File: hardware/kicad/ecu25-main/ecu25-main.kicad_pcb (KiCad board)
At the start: 2 copper layers, 200 x 150 mm, 303 parts, among them J1 Screw_Terminal_BATT, J10 Screw_Terminal_RS485, J11 TC2030 SWD, J12 Ribbon 20-way, J13 Screw_Terminal_DPLUS, J14 DEBUG_UART, J2 Screw_Terminal_DIN, J3 Screw_Terminal_SENDERS, J4 Screw_Terminal_MPU, J5 Screw_Terminal_GEN, J6 Screw_Terminal_MAINS, J7 Screw_Terminal_CT, J8 Screw_Terminal_RELAY_OUT, J9 Screw_Terminal_CAN, K1 G5LE-1 24V, K2 G5LE-1 24V, K3 G5LE-1 24V, K4 G5LE-1 24V, K5 G5LE-1 24V, K6 G5LE-1 24V, Q1 SQD50P06-15L, Q3 BC857, Q4 BC857, Q5 BC857, Q60 2N7002K 60V, Q61 2N7002K 60V, Q62 2N7002K 60V, Q63 2N7002K 60V, Q64 2N7002K 60V, Q65 2N7002K 60V, U1 LM5164DDA-Q1, U10 MCP6002, U11 M95M02-DR, U12 STM32F407VGT6, U2 TLV75533 (500mA), U3 LM358, U4 LM358, U5 LM2903, U6 TJA1051T/3, U7 THVD1450, U8 MCP6002, U9 MCP6002, Y1 8MHz, Y2 32.768kHz

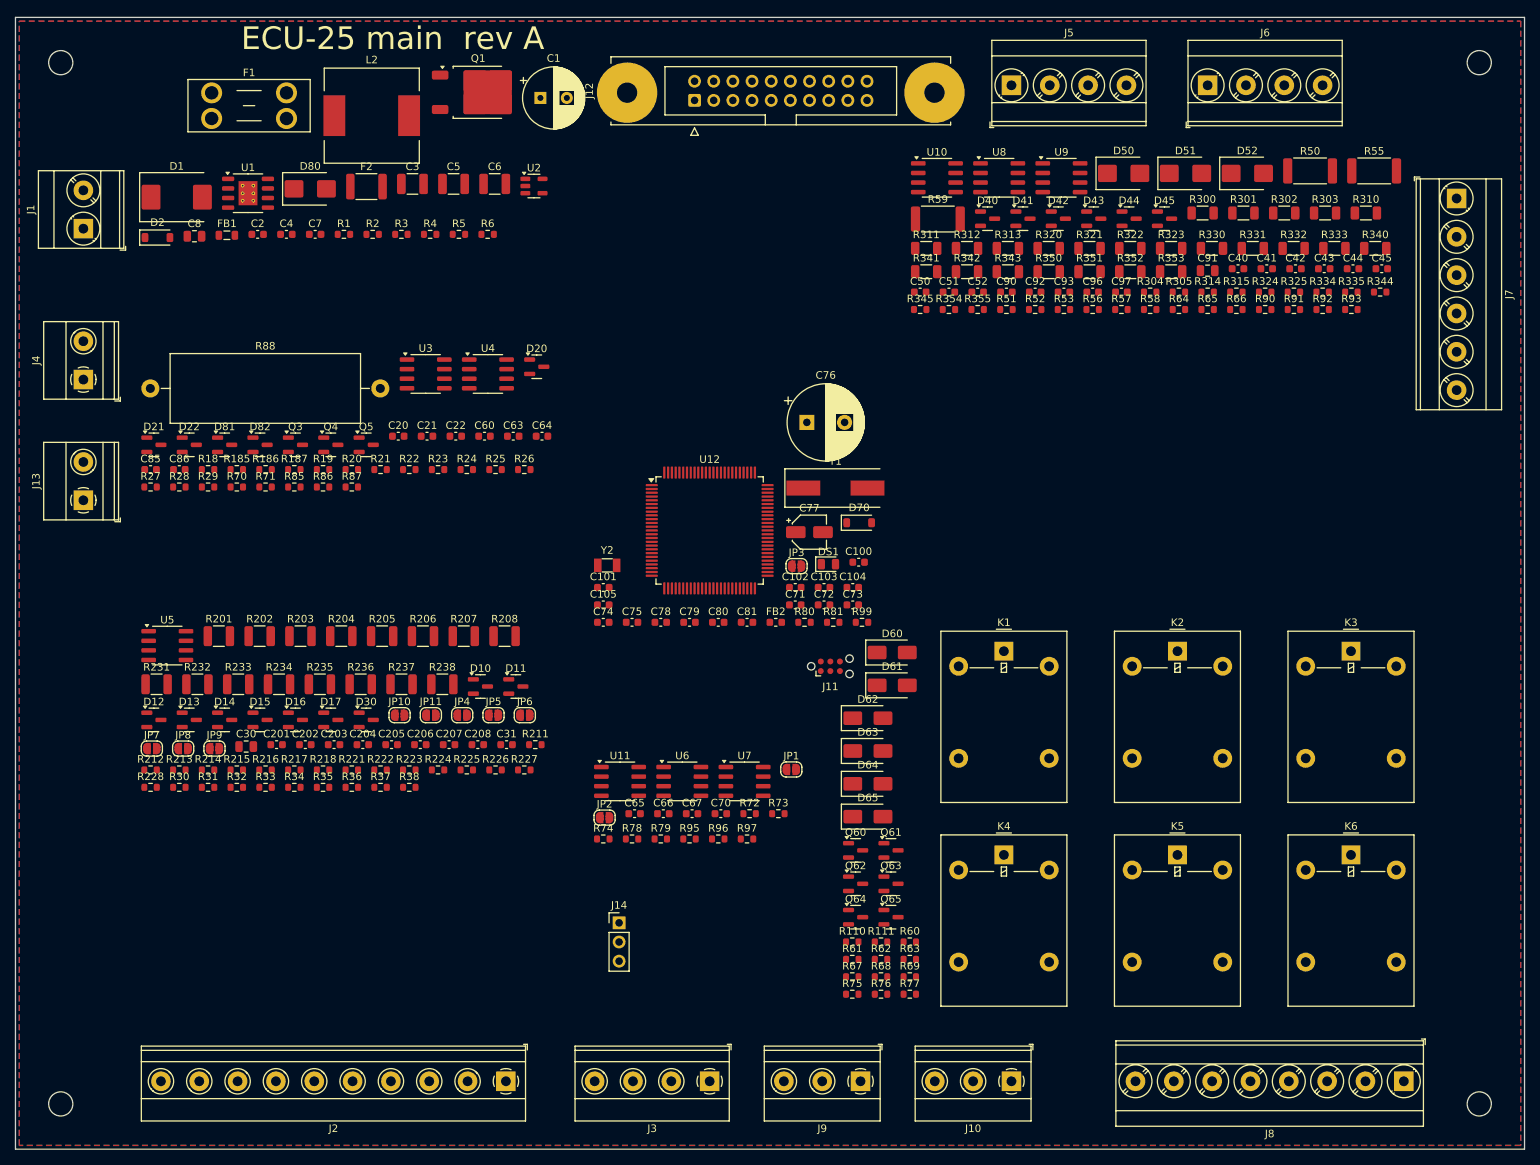
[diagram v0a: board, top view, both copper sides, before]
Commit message: Fix PCB SME review findings: relay pin map, 415V clearances, terminal creepage
CRITICAL: G5LE-1 pin map — lib symbol/footprint has coil on pins 2/5, COM 1,
NO 3, NC 4; generator assumed 1/2 coil + 3/4/5 contacts, netting all six
relays dead (coil open, outputs on NC, volt-free GEN/MAINS contacts tied to
logic GND through the driver FETs). Relay sheet rewired, verified by netlist.

MAJOR fixes, all generator-side:
- Volt-free contactor pairs split off J8 onto new J15; J5/J6/J15 are 8-pole
  5.08mm blocks with only odd poles wired (10.16mm live pitch) + pad remap —
  fully-populated 400V-class blocks don't meet PD2 creepage for 415V L-L /
  unsynchronized-source spacing
- DRU rebuilt: GND no longer swept into the line class (was making the board
  unroutable), 3.0mm line class now includes the J15 contactor nets, per-chain
  1.0mm exemptions so the first 330k doesn't false-trip, netless-pad rule,
  generated-file header
- Copper-pour keepouts under J5/J6, the 330k chains, and the volt-free
  contact corridor K3/K4 -> J15
- CT burden + TVS fixed at J7; buck hot loop (C3/U1/L2/C5/C6) and input chain
  fixed in electrical order; R88 (2.6W) moved to the board edge away from
  precision analog; packer margin 0.4 -> 0.6mm
- F2 PTC now specified 60V (sees the 53V load-dump clamp while tripped)

Docs + diagrams + PDFs synced; verified: no overlaps, nothing outside
outline, odd-pole remap correct on J5/J6/J15, netlist sweep clean
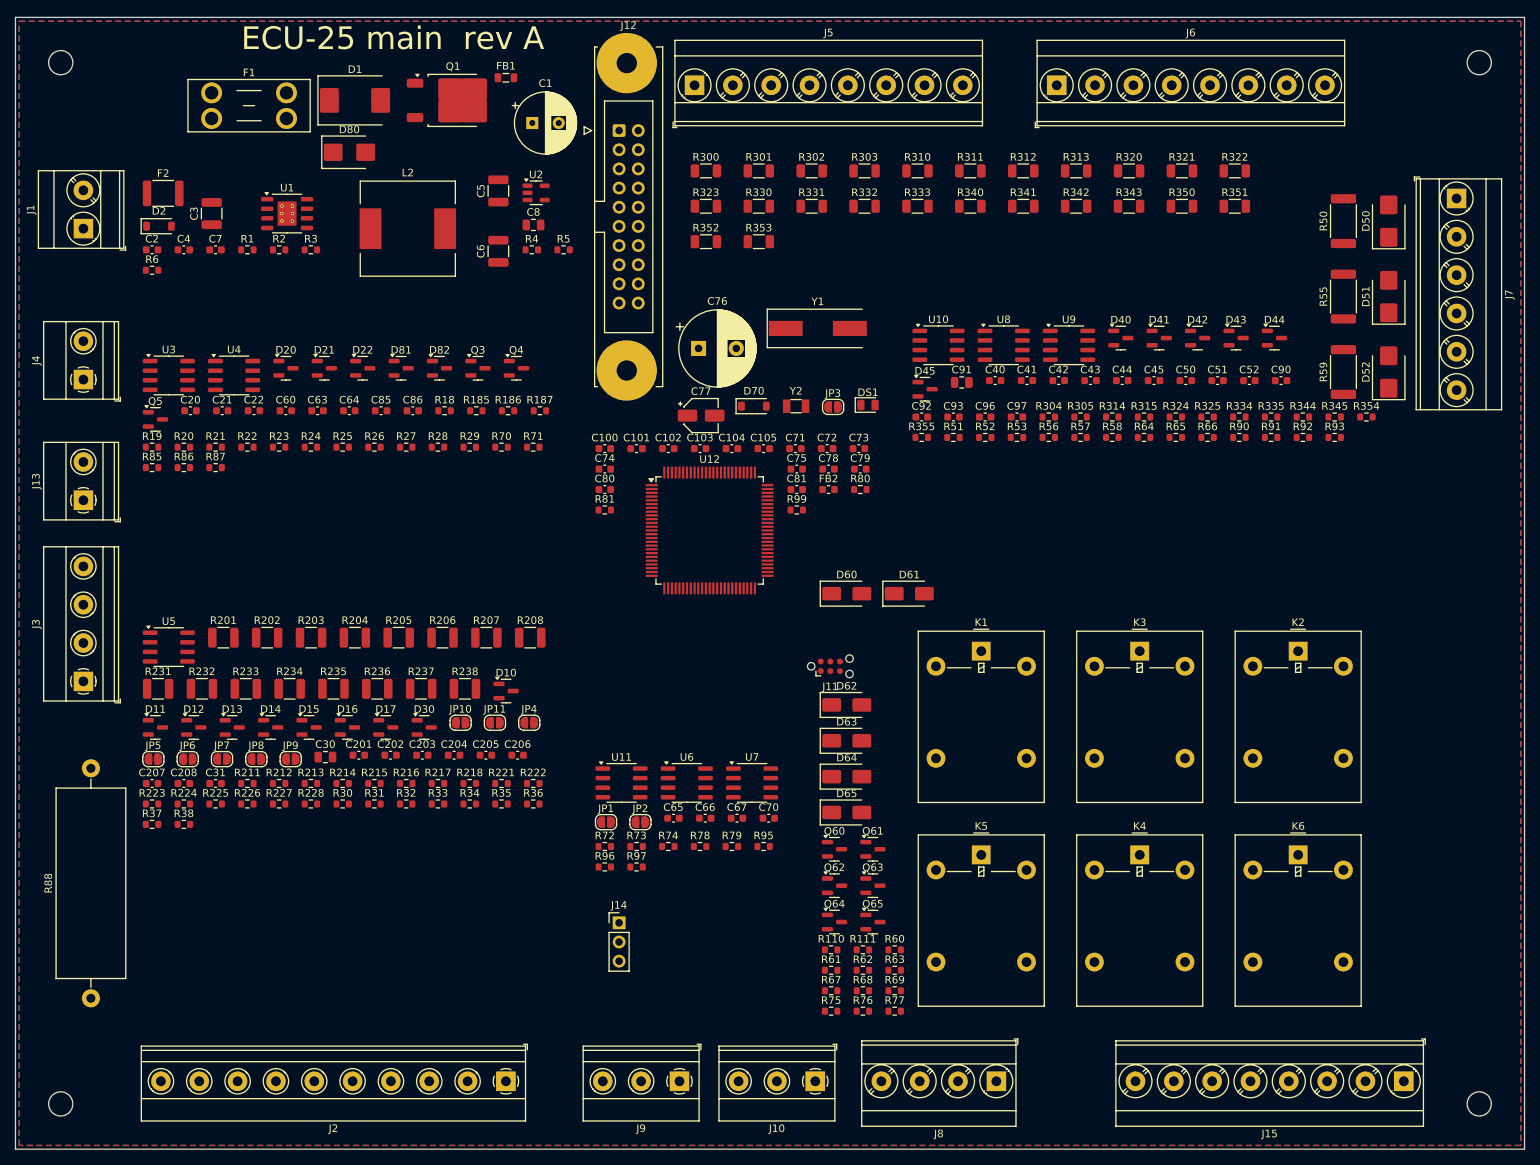
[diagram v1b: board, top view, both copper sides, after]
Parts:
- added J15: Screw_Terminal_CONTACTOR, TerminalBlock_Phoenix_MKDS-3-8-5.08_1x08_P5.08mm_Horizontal, F.Cu at (204.0, 161.0)
- F2: value PTC 1.1A -> PTC 1.1A 60V
- J5, J6: footprint TerminalBlock_Phoenix_MKDS-3-4-5.08_1x04_P5.08mm_Horizontal -> TerminalBlock_Phoenix_MKDS-3-8-5.08_1x08_P5.08mm_Horizontal
- J8: footprint TerminalBlock_Phoenix_MKDS-3-8-5.08_1x08_P5.08mm_Horizontal -> TerminalBlock_Phoenix_MKDS-3-4-5.08_1x04_P5.08mm_Horizontal
- moved J3 98.5 mm to (29.0, 108.0), turned to 90 degrees
- moved R88 81.2 mm to (30.0, 150.0), turned to 90 degrees
- moved R300 66.1 mm to (111.5, 40.3)
- moved R301 64.5 mm to (118.5, 40.3)
- moved R302 62.9 mm to (125.5, 40.3)
- moved R323 61.9 mm to (111.5, 45.0)
- moved R303 61.3 mm to (132.5, 40.3)
- moved R330 60.3 mm to (118.5, 45.0)
- moved R310 59.7 mm to (139.5, 40.3)
- moved R331 58.7 mm to (125.5, 45.0)
- moved R59 57.5 mm to (196.0, 67.0), turned to 90 degrees
- moved R354 57.1 mm to (199.0, 73.0)
- moved R332 57.1 mm to (132.5, 45.0)
- moved R345 56.7 mm to (194.8, 73.0)
- moved R352 56.4 mm to (111.5, 49.7)
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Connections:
- J5 pad 2: /AC sensing/AC_GEN_L2 -> (no net)
- J5 pad 3: /AC sensing/AC_GEN_L3 -> /AC sensing/AC_GEN_L2
- J5 pad 4: GND -> (no net)
- J6 pad 2: /AC sensing/AC_MAINS_L2 -> (no net)
- J6 pad 3: /AC sensing/AC_MAINS_L3 -> /AC sensing/AC_MAINS_L2
- J6 pad 4: GND -> (no net)
- K1 pad 1: Net-(D60-A) -> +24V_SW
- K1 pad 2: +24V_SW -> Net-(D60-A)
- K1 pad 3: +24V_SW -> /Relay drivers/FUEL_OUT
- K1 pad 4: /Relay drivers/FUEL_OUT -> unconnected-(K1-Pad4)
- K1 pad 5: unconnected-(K1-Pad5) -> +24V_SW
- K2 pad 1: Net-(D61-A) -> +24V_SW
- K2 pad 2: +24V_SW -> Net-(D61-A)
- K2 pad 3: +24V_SW -> /Relay drivers/START_OUT
- K2 pad 4: /Relay drivers/START_OUT -> unconnected-(K2-Pad4)
- K2 pad 5: unconnected-(K2-Pad5) -> +24V_SW
- K3 pad 1: Net-(D62-A) -> /Relay drivers/GEN_COM
- K3 pad 2: +24V_SW -> Net-(D62-A)
- K3 pad 3: /Relay drivers/GEN_COM -> /Relay drivers/GEN_NO
- K3 pad 4: /Relay drivers/GEN_NO -> unconnected-(K3-Pad4)
- K3 pad 5: unconnected-(K3-Pad5) -> +24V_SW
- K4 pad 1: Net-(D63-A) -> /Relay drivers/MAINS_COM
- K4 pad 2: +24V_SW -> Net-(D63-A)
- K4 pad 3: /Relay drivers/MAINS_COM -> /Relay drivers/MAINS_NO
- K4 pad 4: /Relay drivers/MAINS_NO -> unconnected-(K4-Pad4)
- K4 pad 5: unconnected-(K4-Pad5) -> +24V_SW
- K5 pad 1: Net-(D64-A) -> +24V_SW
- K5 pad 2: +24V_SW -> Net-(D64-A)
- K5 pad 3: +24V_SW -> /Relay drivers/HORN_OUT
- K5 pad 4: /Relay drivers/HORN_OUT -> unconnected-(K5-Pad4)
- K5 pad 5: unconnected-(K5-Pad5) -> +24V_SW
- K6 pad 1: Net-(D65-A) -> +24V_SW
- K6 pad 2: +24V_SW -> Net-(D65-A)
- K6 pad 3: +24V_SW -> /Relay drivers/PREHEAT_OUT
- K6 pad 4: /Relay drivers/PREHEAT_OUT -> unconnected-(K6-Pad4)
- K6 pad 5: unconnected-(K6-Pad5) -> +24V_SW

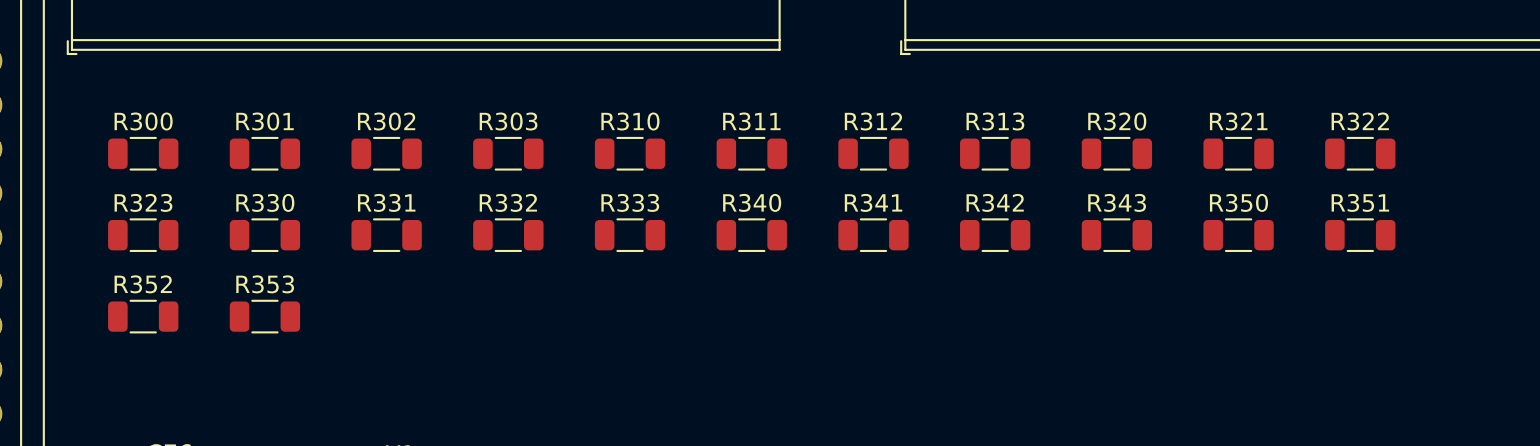
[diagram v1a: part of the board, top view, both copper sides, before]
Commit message: Fix verification-pass findings: rule-area pads flag, corridor width, chain pitch
- Rule areas: SetDoNotAllowPads/Footprints(False) — KiCad default True made
  every pad inside a keepout a DRC error (107 hits)
- J15 corridor keepout widened 208 -> 209mm: GND pour edge was 2.70mm from
  J15 pad 1 vs the 3.0mm rule
- AC-HV strip packing margin 1.2 -> 1.3mm: chain columns packed 2.94-2.96mm
  pad-to-pad, 40-60um under the line-class rule (12 DRC hits)
- Loud warning on PAD_REMAP: 'Update PCB from Schematic' would silently move
  J5/J6/J15 nets back to pads 1-4 — board is regenerate-only
- DRC re-run: 0 clearance violations, 0 keepout violations; remaining items
  are the documented pre-existing set (unrouted ratsnest, lib footprint
  thermal-via drills, silk overlaps)
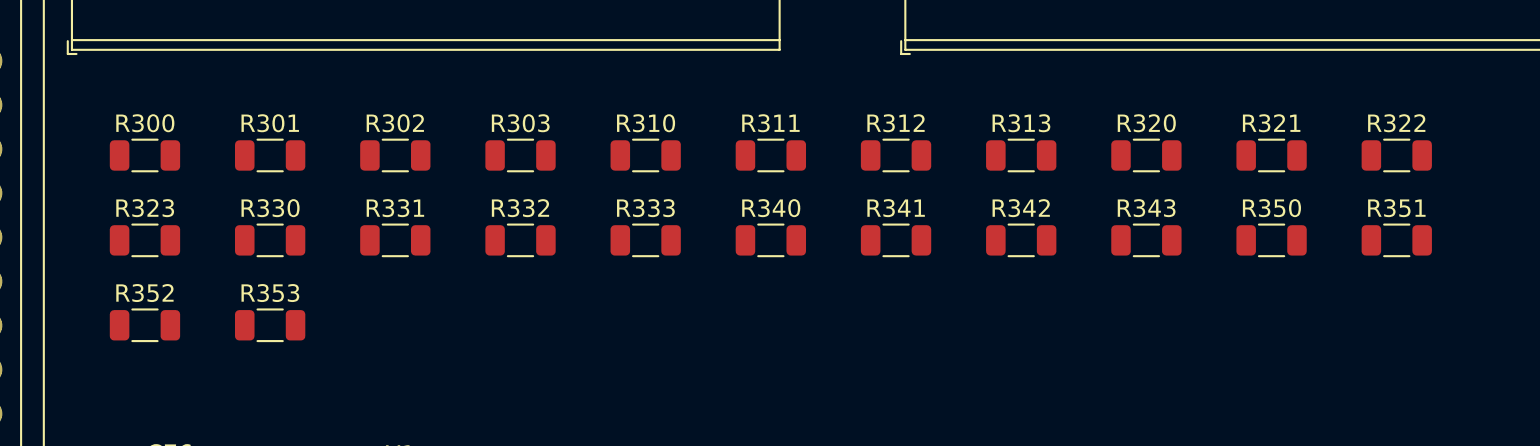
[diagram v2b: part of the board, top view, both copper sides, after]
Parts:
- moved R351 2.12 mm to (183.7, 45.3)
- moved R322 2.10 mm to (183.7, 40.4)
- moved R350 1.92 mm to (176.5, 45.3)
- moved R321 1.90 mm to (176.5, 40.4)
- moved R343 1.73 mm to (169.3, 45.3)
- moved R320 1.70 mm to (169.3, 40.4)
- moved R342 1.53 mm to (162.1, 45.3)
- moved R313 1.50 mm to (162.1, 40.4)
- moved R341 1.33 mm to (154.9, 45.3)
- moved R312 1.30 mm to (154.9, 40.4)
- moved R340 1.14 mm to (147.7, 45.3)
- moved R311 1.10 mm to (147.7, 40.4)
- moved R333 0.95 mm to (140.4, 45.3)
- moved R310 0.91 mm to (140.4, 40.4)
- moved R332 0.76 mm to (133.2, 45.3)
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
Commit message: Add BOM generator + breadboard prototyping guide; fix parts found by review
New:
- gen_bom.py: builds docs/bom/ecu25-main-bom.{md,csv} from the netlist —
  300 components in 91 order lines, grouped by orderable value + package,
  with part numbers for the actives and a shared-across-sheets section
- docs/bom/breadboard-prototype.md: through-hole translation in eight blocks
  (digital input, relay driver, sender current source, VREF buffer, MPU
  comparator, CT, AC sense, comms), each with an explicit node list, a
  reference-schematic link, and a test that proves that block. Safety rules
  for the 415V sensing (not on a breadboard), CT open-circuit, grounding,
  and supply current limiting

Design corrections the BOM review reached back into:
- F2 was specified as a 60V 1812 PPTC that does not exist (the 0ZCJ0110 is
  8V/1206) -> RXEF110, 72V radial, on Fuse_Bourns_MF-RG900 (1.01mm drill for
  its 0.81mm leads)
- C1 50V -> 63V and C2 50V -> 100V: both sit on +24V, which D1 clamps to ~53V
- CT gain pairs (R51/R52, R56/R57, R64/R65) and the phase-match resistors
  (R53/R58/R66) now carry explicit 1% — 5% pairs would give up to 7% gain
  error on every current and power reading
- G5LE-1-DC24 coil is 1.44k / 400mW / 16.7mA, not 360R / 67mA: a 4x error
  that had propagated through three documents. Every sizing decision was made
  against the larger number, so all of them keep margin
- F2 also gates the four switched outputs, not just the coils — documented

Board:
- Netclasses in .kicad_pro (Battery/Power/Logic/GND/HV_AC/HV_CHAIN) with
  track widths and clearances; +3V3/+5V split into Logic because the
  LQFP-100's own pads are 0.2mm apart and cannot take a wide clearance class
- GND pour fills at the widest non-HV class, with keepouts around every NPTH
  barrel; minimum through-drill 0.2mm to match U1's library thermal vias
- Board now reports zero DRC errors (unrouted ratsnest and silk warnings
  aside), no courtyard overlaps, nothing outside the outline

Also: route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
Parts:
- C1: value 100uF 50V -> 100uF 63V; footprint CP_Radial_D8.0mm_P3.50mm -> CP_Radial_D10.0mm_P5.00mm
- C2: value 100nF 50V -> 100nF 100V; footprint C_0603_1608Metric -> C_0805_2012Metric
- F2: value PTC 1.1A 60V -> PTC 1.1A 72V; footprint Fuse_1812_4532Metric -> Fuse_Bourns_MF-RG900
- R51, R52, R56, R57, R64, R65: value 10k -> 10k 1%
- R53, R58, R66: value 6.8k (phase match) -> 6.8k 1% (phase match)
- moved R5 54.8 mm to (38.1, 45.8)
- moved R6 50.9 mm to (88.4, 45.8)
- moved C1 48.3 mm to (46.0, 57.0)
- moved C4 42.9 mm to (83.1, 37.4)
- moved C7 42.9 mm to (87.3, 37.4)
- moved R1 42.9 mm to (91.5, 37.4)
- moved C2 38.3 mm to (74.0, 37.6)
- moved D2 31.3 mm to (68.7, 37.8)
- moved R3 30.3 mm to (88.4, 43.1)
- moved U2 26.4 mm to (63.0, 38.5)
- moved R2 18.5 mm to (38.1, 43.1)
- moved C8 14.1 mm to (78.7, 37.6)
- moved R4 8.78 mm to (92.6, 43.1)
- moved D80 8.25 mm to (56.1, 38.9)
- moved F2 5.82 mm to (41.3, 37.8)
